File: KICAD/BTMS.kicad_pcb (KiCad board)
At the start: 4 copper layers, 126.2 x 137.4 mm, 304 parts, among them J1 fan, J10 U1COMMS, J11 U2COMMS, J13 IntBTemp, J14 ctrlTemp, J15 12Vout, J16 12Vin, J17 5Vout, J2 mContactor, J3 Tac, J5 ICSP, J7 5Vout, J9 key, Q1 PSMN5R6-100BS, Q10 PSMN5R6-100BS, Q11 DMN65D8L, Q12 DMN65D8L, Q13 FDN340P, Q14 ZXTP2025FTA, Q15 ZXTP2025FTA, Q16 ZXTP2025FTA, Q18 DMN65D8L, Q2 PSMN5R6-100BS, Q3 PSMN5R6-100BS, Q4 DMN65D8L, Q5 DMN65D8L, Q6 DMN65D8L, Q7 DMN65D8L, Q8 PSMN5R6-100BS, Q9 FDN340P, U1 R-78HB12-0.5, U10 A41AS12VDC, U11 A41AS12VDC, U12 A41AS12VDC, U13 A41AS12VDC, U14 A41AS12VDC, U15 NL17SZ74USG, U2 ACS780xLRTR-050B, U3 UCC27201DDAR, U4 FAN3111ESX, U5 HCPL-3120, U6 L7805CV, U7 LTV-817S, U8 dsPIC30F3011-PT, U9 LM62CIM3/NOPB

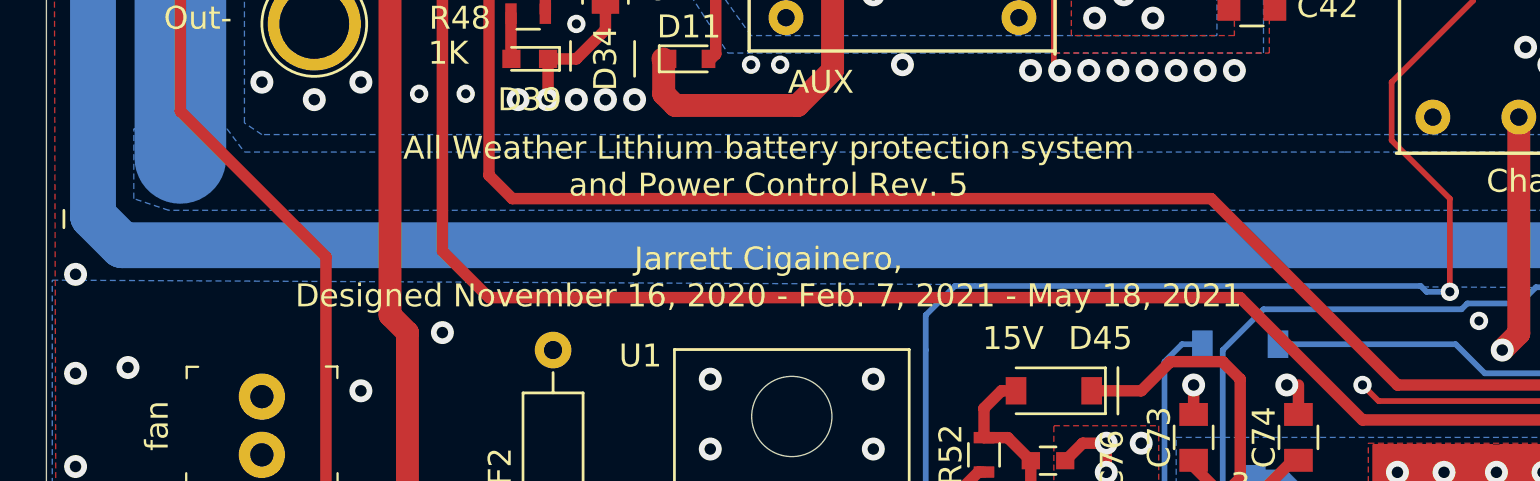
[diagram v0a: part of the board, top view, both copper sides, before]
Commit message: Created PDF schematic and updated Silkscreen on board layout.
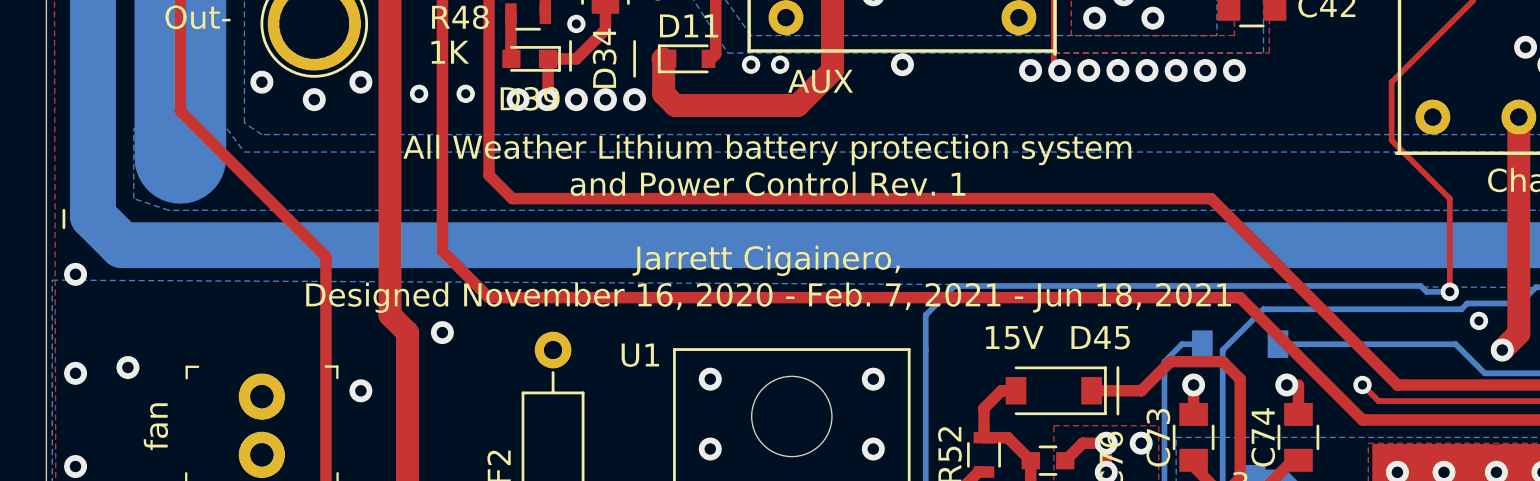
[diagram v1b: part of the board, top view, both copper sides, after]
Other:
- board text added: "All Weather Lithium battery protection system and Power Control Rev. 1 Jarrett Cigainero, Designed November 16, 2020 - Feb. 7, 2021 - Jun 18, 2021"
- board text removed: "All Weather Lithium battery protection system and Battery Control Rev. 5 Jarrett Cigainero, Designed November 16, 2020 - Feb. 7, 2021"
- board text removed: "All Weather Lithium battery protection system and Power Control Rev. 5 Jarrett Cigainero, Designed November 16, 2020 - Feb. 7, 2021 - May 18, 2021"
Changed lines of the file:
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@@
     (effects (font (size 0.8 0.8) (thickness 0.125)))
   )
-  (gr_text "All Weather Lithium battery protection system\nand Power Control Rev. 5\n\nJarrett Cigainero, \nDesigned November 16, 2020 - Feb. 7, 2021 - May 18, 2021" (at 62.484 127) (layer F.SilkS)
+  (gr_text "All Weather Lithium battery protection system\nand Power Control Rev. 1\n\nJarrett Cigainero, \nDesigned November 16, 2020 - Feb. 7, 2021 - Jun 18, 2021" (at 62.484 127) (layer F.SilkS)
     (effects (font (size 1 1) (thickness 0.15)))
   )
@@
   (gr_poly (pts (xy 97.536 131.572) (xy 96.266 131.572) (xy 96.266 132.588) (xy 94.488 132.588) (xy 94.488 131.572) (xy 95.25 131.572) (xy 95.25 130.81) (xy 96.266 130.81) (xy 96.266 129.54) (xy 97.536 129.54)) (layer B.SilkS) (width 0.1))
   (gr_poly (pts (xy 91.186 130.81) (xy 92.202 130.81) (xy 92.202 131.572) (xy 92.964 131.572) (xy 92.964 132.588) (xy 91.186 132.588) (xy 91.186 131.572) (xy 89.916 131.572) (xy 89.916 129.54) (xy 91.186 129.54)) (layer B.SilkS) (width 0.1))
-  (gr_text "All Weather Lithium battery protection system\nand Battery Control Rev. 5\n\n\nJarrett Cigainero, \nDesigned November 16, 2020 - Feb. 7, 2021" (at 124.206 141.224) (layer B.SilkS)
+  (gr_text "All Weather Lithium battery protection system\nand Power Control Rev. 1\n\nJarrett Cigainero, \nDesigned November 16, 2020 - Feb. 7, 2021 - Jun 18, 2021" (at 125.222 141.986) (layer B.SilkS)
     (effects (font (size 1 1) (thickness 0.15)) (justify mirror))
   )
-  (gr_text "An abomination of EE..." (at 78.486 139.954) (layer B.SilkS)
+  (gr_text "An abomination of EE..." (at 68.58 141.478) (layer B.SilkS)
     (effects (font (size 1 1) (thickness 0.15)) (justify mirror))
   )

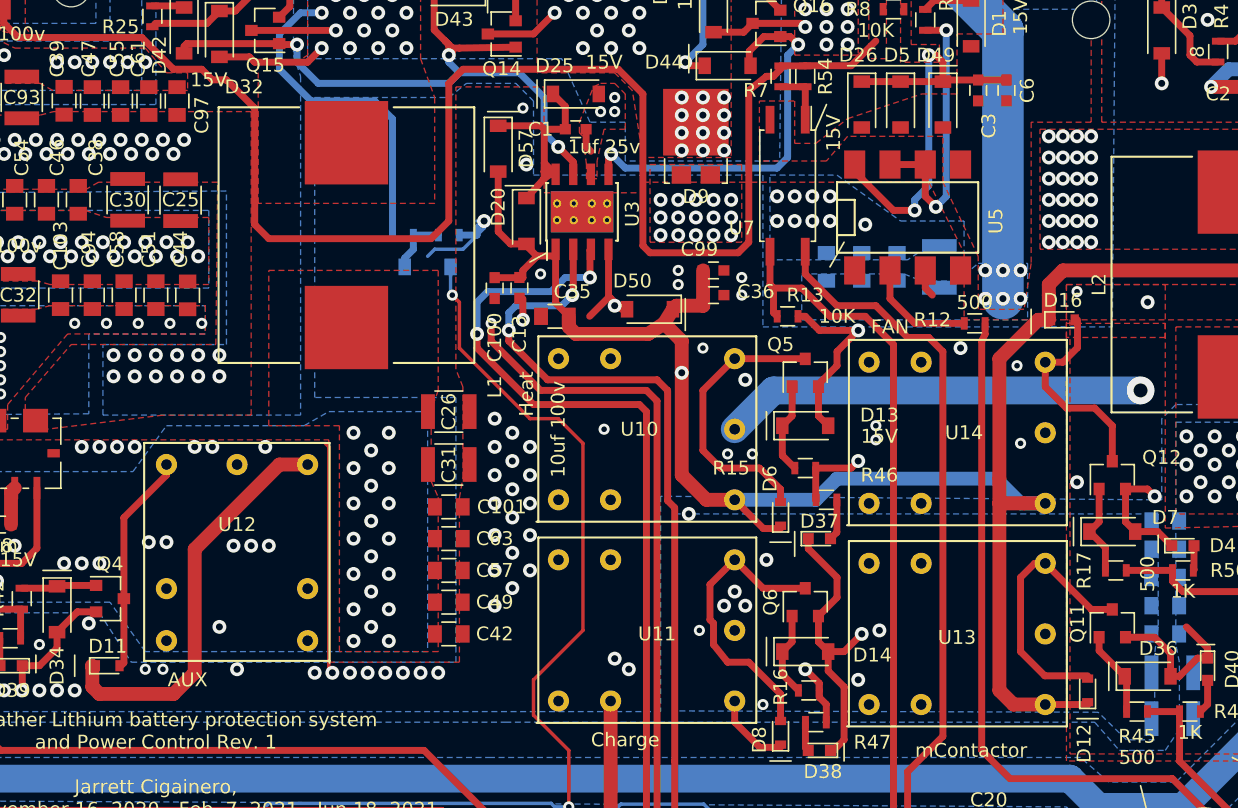
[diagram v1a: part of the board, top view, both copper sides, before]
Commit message: Updated board layout to reflect schematic.
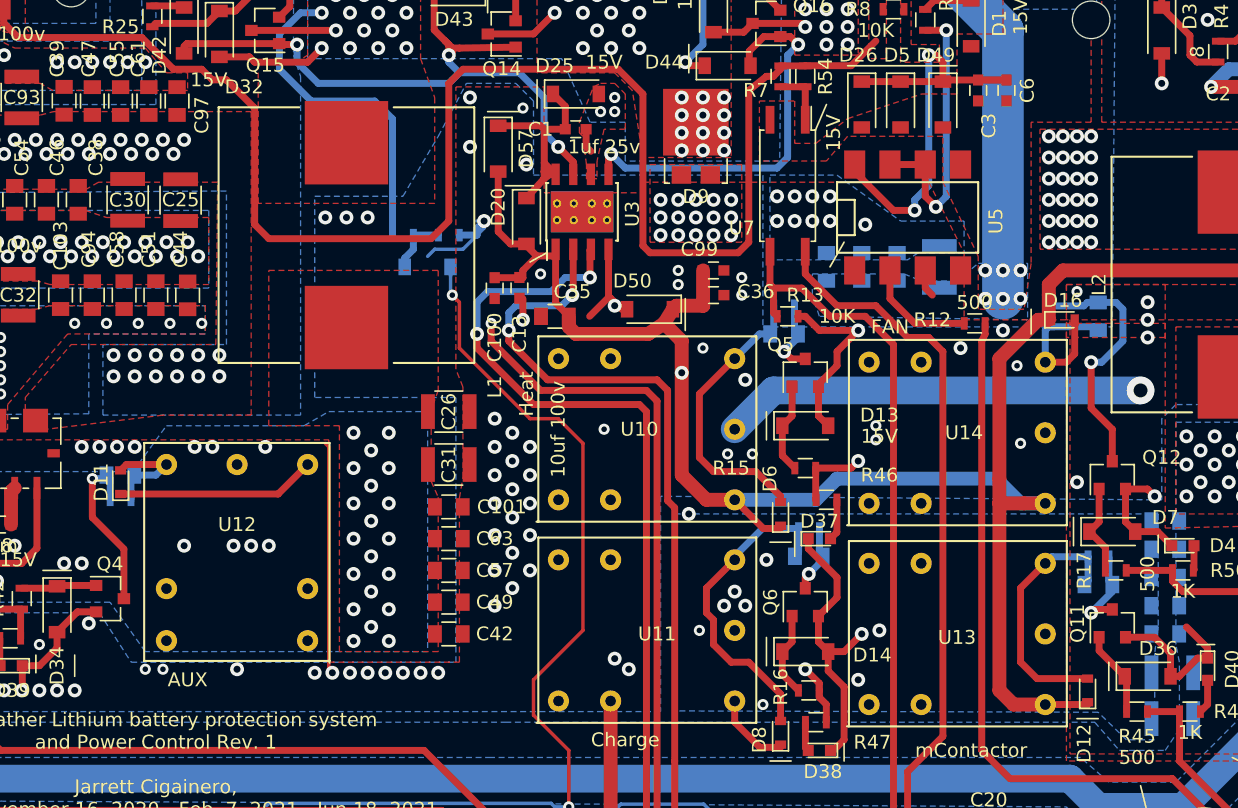
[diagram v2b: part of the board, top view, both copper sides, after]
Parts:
- added C111: 10uf 25v, Capacitors_SMD:C_0805, B.Cu at (107.7, 96.0)
- added C112: 10uf 25v, Capacitors_SMD:C_0805, B.Cu at (109.5, 112.0)
- added C113: 10uf 25v, Capacitors_SMD:C_0805, B.Cu at (59.9, 106.2)
- added C114: 10uf 25v, Capacitors_SMD:C_0805, B.Cu at (130.3, 114.0)
- added C115: 10uf 25v, Capacitors_SMD:C_0805, B.Cu at (130.3, 94.7)
- added R62: 500, Resistors_SMD:R_0603, B.Cu at (107.7, 94.0)
- added R64: 500, Resistors_SMD:R_0603, B.Cu at (109.5, 110.0)
- added R65: 500, Resistors_SMD:R_0603, B.Cu at (59.9, 108.0)
- added R66: 500, Resistors_SMD:R_0603, B.Cu at (130.3, 112.0)
- added R67: 500, Resistors_SMD:R_0603, B.Cu at (126.7, 94.7)
- moved D11 13.2 mm to (59.9, 106.7), turned to 90 degrees
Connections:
- D11 pad 2: Net-(D11-Pad2) -> Net-(C113-Pad1)
- D12 pad 2: Net-(D12-Pad2) -> Net-(C114-Pad1)
- D16 pad 2: Net-(D16-Pad2) -> Net-(C115-Pad1)
- D6 pad 2: Net-(D6-Pad2) -> Net-(C111-Pad1)
- D8 pad 2: Net-(D8-Pad2) -> Net-(C112-Pad1)
- Q11 pad 3: Net-(D12-Pad2) -> Net-(C114-Pad2)
- Q12 pad 3: Net-(D16-Pad2) -> Net-(C115-Pad2)
- Q4 pad 3: Net-(D11-Pad2) -> Net-(C113-Pad2)
- Q5 pad 3: Net-(D6-Pad2) -> Net-(C111-Pad2)
- Q6 pad 3: Net-(D8-Pad2) -> Net-(C112-Pad2)
- U10 pad 1: Net-(D6-Pad2) -> Net-(C111-Pad1)
- U11 pad 1: Net-(D8-Pad2) -> Net-(C112-Pad1)
- U12 pad 1: Net-(D11-Pad2) -> Net-(C113-Pad1)
- U13 pad 1: Net-(D12-Pad2) -> Net-(C114-Pad1)
- U14 pad 1: Net-(D16-Pad2) -> Net-(C115-Pad1)
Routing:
- net Net-(C112-Pad1): track 0.00 -> 23.2 mm
- net Net-(C111-Pad1): track 0.00 -> 21.0 mm
- net Net-(D8-Pad2): track 21.0 -> 0.00 mm
- net Net-(D6-Pad2): track 20.1 -> 0.00 mm
- net Net-(D12-Pad2): track 19.3 -> 0.00 mm
- net Net-(C115-Pad2): track 0.00 -> 18.6 mm, vias 0 -> 1
- net Net-(C114-Pad1): track 0.00 -> 18.6 mm
- net Net-(D11-Pad2): track 15.8 -> 0.00 mm
- net Net-(D16-Pad2): track 15.1 -> 0.00 mm
- net +12V: track 416.9 -> 402.0 mm
- net Net-(C113-Pad2): track 0.00 -> 12.6 mm, vias 0 -> 1
- net Net-(C115-Pad1): track 0.00 -> 11.1 mm
- net Net-(C113-Pad1): track 0.00 -> 7.98 mm
- net Net-(C114-Pad2): track 0.00 -> 6.39 mm, vias 0 -> 1
- net Net-(C111-Pad2): track 0.00 -> 5.56 mm, vias 0 -> 1
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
